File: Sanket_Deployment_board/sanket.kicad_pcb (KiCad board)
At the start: 2 copper layers, 95.9 x 92 mm, 42 parts, among them J2 Conn_02x03_Counter_Clockwise, J3 Conn_02x03_Counter_Clockwise, U1 SN74LVC1G17QDCKRQ1

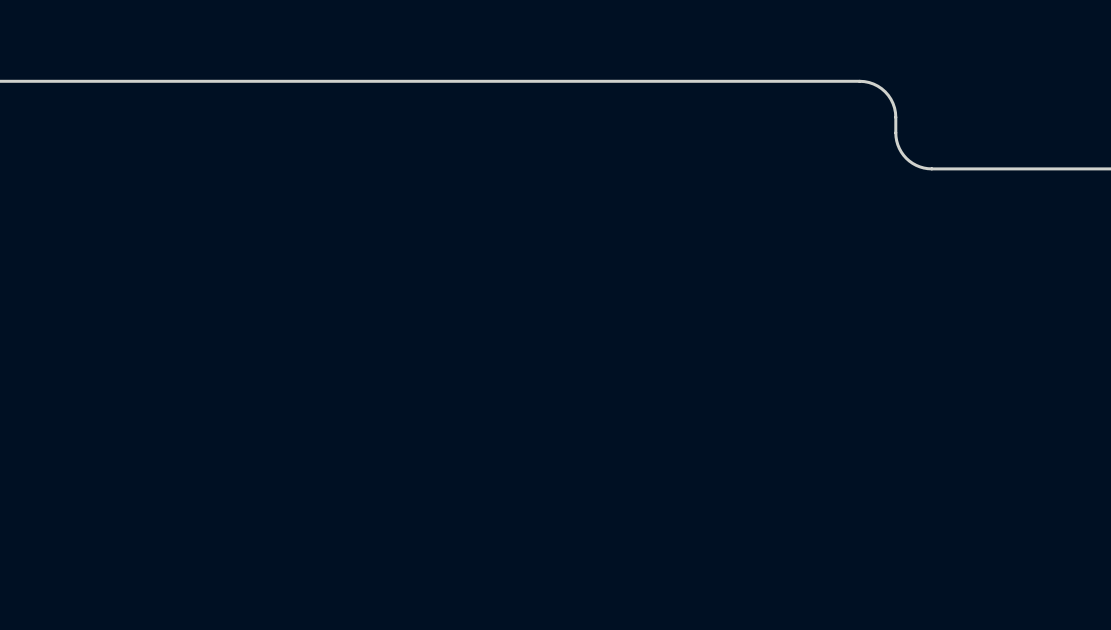
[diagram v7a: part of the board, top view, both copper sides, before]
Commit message: Added schematic pdf of Sanket
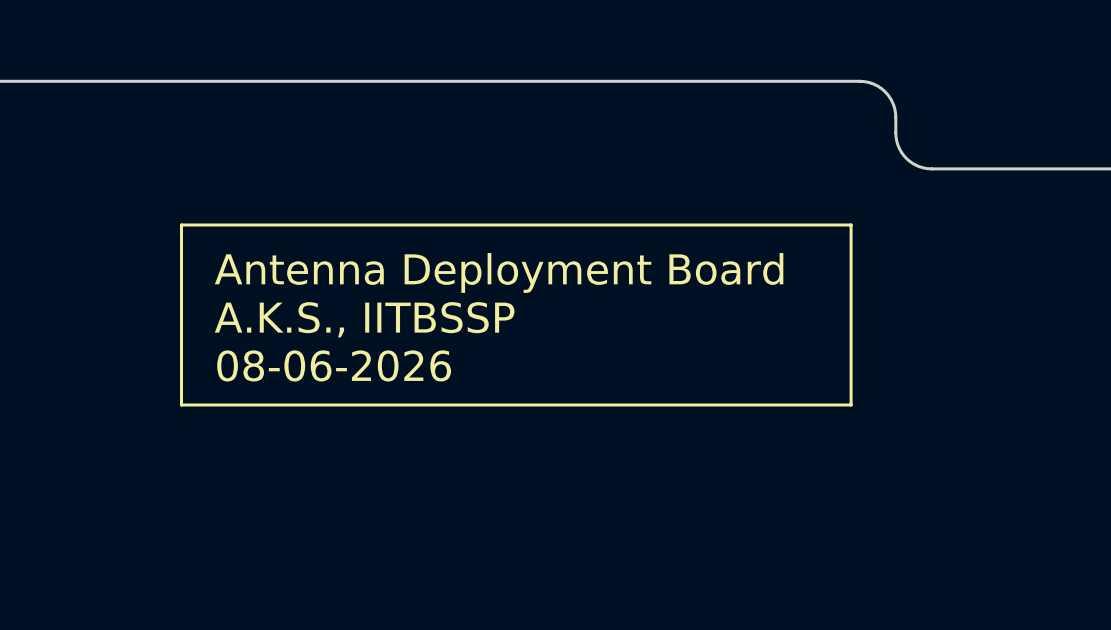
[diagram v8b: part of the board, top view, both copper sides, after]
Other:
- board text added: "Antenna Deployment Board A.K.S., IITBSSP 08-06-2026"
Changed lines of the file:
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@@
 	(paper "A4")
 	(title_block
-		(title "Antenna Deployment Board")
+		(title "ADS")
 		(date "2025-07-10")
 		(rev "6")
 		(company "IITBSSP")
+		(comment 1 "Author: A.K.S.")
 	)
 	(layers
@@
 		(embedded_fonts no)
 	)
+	(gr_rect
+		(start 114.4911 62.0886)
+		(end 136.8111 68.0886)
+		(stroke
+			(width 0.1)
+			(type default)
+		)
+		(fill no)
+		(layer "F.SilkS")
+	)
 	(gr_line
 		(start 100.4911 58.4986)
@@
 		(layer "Edge.Cuts")
 	)
+	(gr_text "Antenna Deployment Board\nA.K.S., IITBSSP\n08-06-2026"
+		(at 115.5911 67.4086 0)
+		(layer "F.SilkS")
+		(effects
+			(font
+				(size 1 1)
+				(thickness 0.1)
+			)
+			(justify left bottom)
+		)
+	)
 	(gr_text "12V"
 		(at 116.2411 131.0486 0)
@@
 	)
 	(zone
-		(net "/BurnWire1OUT")
+		(net "+3V3")
 		(layer "F.Cu")
 		(hatch none 0.1)
-		(priority 30001)
+		(priority 30004)
 		(attr
 			(teardrop
@@
 		(polygon
 			(pts
-				(xy 174.922166 106.9386) (xy 174.922166 105.9386) (xy 173.473001 105.625201) (xy 173.221166 106.4386)
-				(xy 173.473001 107.251999)
+				(xy 126.727839 128.802772) (xy 126.727839 129.202772) (xy 127.286114 129.300205) (xy 127.328839 129.002772)
+				(xy 127.286114 128.705339)
 			)
 		)
 	)
 	(zone
-		(net "/BurnWire1OUT")
+		(net "+12V")
 		(layer "F.Cu")
 		(hatch none 0.1)
-		(priority 30002)
+		(priority 30000)
 		(attr
 			(teardrop
@@
 		(polygon
 			(pts
-				(xy 174.070352 105.9386) (xy 174.070352 106.9386) (xy 175.519517 107.251999) (xy 175.771352 106.4386)
-				(xy 175.519517 105.625201)
+				(xy 107.105694 133.941113) (xy 106.398587 133.234006) (xy 104.949018 134.1886) (xy 105.300393 135.039307)
+				(xy 106.1511 135.390682)
 			)
 		)
 	)
 	(zone
-		(net "+12V")
+		(net "+3V3")
 		(layer "F.Cu")
 		(hatch none 0.1)
-		(priority 30000)
+		(priority 30007)
 		(attr
 			(teardrop
@@
 		(polygon
 			(pts
-				(xy 107.105694 133.941113) (xy 106.398587 133.234006) (xy 104.949018 134.1886) (xy 105.300393 135.039307)
-				(xy 106.1511 135.390682)
+				(xy 125.965041 135.650338) (xy 126.106462 135.791759) (xy 126.573005 135.575764) (xy 126.460722 135.296078)
+				(xy 126.181036 135.183795)
 			)
 		)
 	)
 	(zone
-		(net "+3V3")
+		(net "/BurnWire1OUT")
 		(layer "F.Cu")
 		(hatch none 0.1)
-		(priority 30006)
+		(priority 30001)
 		(attr
 			(teardrop
@@
 		(polygon
 			(pts
-				(xy 125.3711 138.401167) (xy 125.1711 138.401167) (xy 124.993936 138.883795) (xy 125.2711 139.002167)
-				(xy 125.548264 138.883795)
+				(xy 174.922166 106.9386) (xy 174.922166 105.9386) (xy 173.473001 105.625201) (xy 173.221166 106.4386)
+				(xy 173.473001 107.251999)
 			)
 		)
@@
 		(layer "F.Cu")
 		(hatch none 0.1)
-		(priority 30005)
+		(priority 30006)
 		(attr
 			(teardrop
@@
 		(polygon
 			(pts
-				(xy 123.192127 127.61247) (xy 123.47497 127.329627) (xy 123.149106 126.865972) (xy 122.908578 127.046078)
-				(xy 122.728472 127.286606)
+				(xy 125.3711 138.401167) (xy 125.1711 138.401167) (xy 124.993936 138.883795) (xy 125.2711 139.002167)
+				(xy 125.548264 138.883795)
 			)
 		)
 	)
 	(zone
-		(net "+3V3")
+		(net "Net-(J1-Pin_1)")
 		(layer "F.Cu")
 		(hatch none 0.1)
-		(priority 30004)
+		(priority 30003)
 		(attr
 			(teardrop
@@
 		(polygon
 			(pts
-				(xy 126.727839 128.802772) (xy 126.727839 129.202772) (xy 127.286114 129.300205) (xy 127.328839 129.002772)
-				(xy 127.286114 128.705339)
+				(xy 127.9611 129.9286) (xy 127.9611 130.9286) (xy 128.8111 131.2786) (xy 129.6621 130.4286) (xy 128.8111 129.6286)
 			)
 		)
 	)
 	(zone
-		(net "Net-(J1-Pin_1)")
+		(net "+3V3")
 		(layer "F.Cu")
 		(hatch none 0.1)
-		(priority 30003)
+		(priority 30005)
 		(attr
 			(teardrop
@@
 		(polygon
 			(pts
-				(xy 127.9611 129.9286) (xy 127.9611 130.9286) (xy 128.8111 131.2786) (xy 129.6621 130.4286) (xy 128.8111 129.6286)
+				(xy 123.192127 127.61247) (xy 123.47497 127.329627) (xy 123.149106 126.865972) (xy 122.908578 127.046078)
+				(xy 122.728472 127.286606)
 			)
 		)
 	)
 	(zone
-		(net "+3V3")
+		(net "/BurnWire1OUT")
 		(layer "F.Cu")
 		(hatch none 0.1)
-		(priority 30007)
+		(priority 30002)
 		(attr
 			(teardrop
@@
 		(polygon
 			(pts
-				(xy 125.965041 135.650338) (xy 126.106462 135.791759) (xy 126.573005 135.575764) (xy 126.460722 135.296078)
-				(xy 126.181036 135.183795)
+				(xy 174.070352 105.9386) (xy 174.070352 106.9386) (xy 175.519517 107.251999) (xy 175.771352 106.4386)
+				(xy 175.519517 105.625201)
 			)
 		)
@@
 		(layer "B.Cu")
 		(hatch none 0.1)
-		(priority 30009)
+		(priority 30008)
 		(attr
 			(teardrop
@@
 		(polygon
 			(pts
-				(xy 122.7111 126.6286) (xy 123.1111 126.6286) (xy 123.4111 126.123627) (xy 122.9111 125.6276) (xy 122.4111 126.123627)
+				(xy 124.1361 125.6386) (xy 124.1361 125.2386) (xy 123.3861 125.1286) (xy 122.9101 125.4386) (xy 123.624165 125.9386)
 			)
 		)
@@
 		(layer "B.Cu")
 		(hatch none 0.1)
-		(priority 30004)
+		(priority 30000)
 		(attr
 			(teardrop
@@
 		(polygon
 			(pts
-				(xy 128.877001 142.907395) (xy 128.169895 143.614501) (xy 128.010796 143.7736) (xy 129.761807 144.499307)
-				(xy 130.061404 143.7736)
+				(xy 133.2361 144.9986) (xy 133.2361 143.9986) (xy 132.5111 143.7736) (xy 129.7601 144.4986) (xy 132.5111 145.2236)
 			)
 		)
@@
 		(layer "B.Cu")
 		(hatch none 0.1)
-		(priority 30007)
+		(priority 30009)
 		(attr
 			(teardrop
@@
 		(polygon
 			(pts
-				(xy 124.4227 141.0416) (xy 124.2227 141.0416) (xy 123.84173 141.695929) (xy 124.3227 142.2676) (xy 124.80367 141.695929)
+				(xy 122.7111 126.6286) (xy 123.1111 126.6286) (xy 123.4111 126.123627) (xy 122.9111 125.6276) (xy 122.4111 126.123627)
 			)
 		)
@@
 		(layer "B.Cu")
 		(hatch none 0.1)
-		(priority 30005)
+		(priority 30011)
 		(attr
 			(teardrop
@@
 		(polygon
 			(pts
-				(xy 125.205854 139.205267) (xy 125.064433 139.063846) (xy 124.137316 139.4076) (xy 124.241693 140.028007)
-				(xy 124.8352 140.159285)
+				(xy 124.777941 139.350338) (xy 124.919362 139.491759) (xy 125.385905 139.275764) (xy 125.273622 138.996078)
+				(xy 124.993936 138.883795)
 			)
 		)
@@
 		(layer "B.Cu")
 		(hatch none 0.1)
-		(priority 30011)
+		(priority 30007)
 		(attr
 			(teardrop
@@
 		(polygon
 			(pts
-				(xy 124.777941 139.350338) (xy 124.919362 139.491759) (xy 125.385905 139.275764) (xy 125.273622 138.996078)
-				(xy 124.993936 138.883795)
+				(xy 124.4227 141.0416) (xy 124.2227 141.0416) (xy 123.84173 141.695929) (xy 124.3227 142.2676) (xy 124.80367 141.695929)
 			)
 		)
@@
 		(layer "B.Cu")
 		(hatch none 0.1)
-		(priority 30008)
+		(priority 30004)
 		(attr
 			(teardrop
@@
 		(polygon
 			(pts
-				(xy 124.1361 125.6386) (xy 124.1361 125.2386) (xy 123.3861 125.1286) (xy 122.9101 125.4386) (xy 123.624165 125.9386)
+				(xy 128.877001 142.907395) (xy 128.169895 143.614501) (xy 128.010796 143.7736) (xy 129.761807 144.499307)
+				(xy 130.061404 143.7736)
 			)
 		)
 	)
 	(zone
-		(net "+3V3")
+		(net "GND")
 		(layer "B.Cu")
 		(hatch none 0.1)
-		(priority 30000)
+		(priority 30001)
 		(attr
 			(teardrop
@@
 		(polygon
 			(pts
-				(xy 133.2361 144.9986) (xy 133.2361 143.9986) (xy 132.5111 143.7736) (xy 129.7601 144.4986) (xy 132.5111 145.2236)
+				(xy 106.853841 129.112966) (xy 106.146734 128.405859) (xy 104.900413 129.208967) (xy 105.297499 129.962201)
+				(xy 106.050733 130.359287)
 			)
 		)
 	)
 	(zone
-		(net "+12V")
+		(net "+3V3")
 		(layer "B.Cu")
 		(hatch none 0.1)
-		(priority 30003)
+		(priority 30005)
 		(attr
 			(teardrop
@@
 		(polygon
 			(pts
-				(xy 107.0011 135.5386) (xy 107.0011 134.5386) (xy 106.1511 134.1886) (xy 105.3001 135.0386) (xy 106.1511 135.8886)
+				(xy 125.205854 139.205267) (xy 125.064433 139.063846) (xy 124.137316 139.4076) (xy 124.241693 140.028007)
+				(xy 124.8352 140.159285)
 			)
 		)
@@
 	)
 	(zone
-		(net "GND")
-		(layer "B.Cu")
-		(hatch edge 0.5)
-		(connect_pads
-			(clearance 0.2)
-		)
-		(min_thickness 0.25)
-		(fill yes
-			(thermal_gap 0.5)
-			(thermal_bridge_width 0.5)
-			(island_removal_mode 0)
-		)
-		(polygon
-			(pts
-				(xy 126.7811 128.3086) (xy 103.635272 128.360661) (xy 102.4011 138.4086) (xy 101.4011 142.5386)
-				(xy 102.97468 148.034891) (xy 114.017939 145.624399) (xy 124.4111 145.6386) (xy 124.5211 145.6386)
-				(xy 127.2411 132.3986)
-			)
-		)
-	)
-	(zone
-		(net "GND")
+		(net "+3V3")
 		(layer "B.Cu")
 		(hatch none 0.1)
-		(priority 30001)
+		(priority 30006)
 		(attr
 			(teardrop
@@
 		(polygon
 			(pts
-				(xy 106.853841 129.112966) (xy 106.146734 128.405859) (xy 104.900413 129.208967) (xy 105.297499 129.962201)
-				(xy 106.050733 130.359287)
+				(xy 124.2227 141.3201) (xy 124.4227 141.3201) (xy 124.81617 140.653271) (xy 124.3227 140.1066) (xy 123.82923 140.653271)
 			)
 		)
@@
 		(layer "B.Cu")
 		(hatch none 0.1)
-		(priority 30006)
+		(priority 30002)
 		(attr
 			(teardrop
@@
 		(polygon
 			(pts
-				(xy 124.2227 141.3201) (xy 124.4227 141.3201) (xy 124.81617 140.653271) (xy 124.3227 140.1066) (xy 123.82923 140.653271)
+				(xy 169.133518 107.284234) (xy 169.840625 107.991341) (xy 171.086946 107.188233) (xy 170.68986 106.434999)
+				(xy 169.936626 106.037913)
 			)
 		)
 	)
 	(zone
-		(net "+3V3")
+		(net "+12V")
 		(layer "B.Cu")
 		(hatch none 0.1)
-		(priority 30002)
+		(priority 30003)
 		(attr
 			(teardrop
@@
 		(polygon
 			(pts
-				(xy 169.133518 107.284234) (xy 169.840625 107.991341) (xy 171.086946 107.188233) (xy 170.68986 106.434999)
-				(xy 169.936626 106.037913)
+				(xy 107.0011 135.5386) (xy 107.0011 134.5386) (xy 106.1511 134.1886) (xy 105.3001 135.0386) (xy 106.1511 135.8886)
+			)
+		)
+	)
+	(zone
+		(net "GND")
+		(layer "B.Cu")
+		(hatch edge 0.5)
+		(connect_pads
+			(clearance 0.2)
+		)
+		(min_thickness 0.25)
+		(fill yes
+			(thermal_gap 0.5)
+			(thermal_bridge_width 0.5)
+			(island_removal_mode 0)
+		)
+		(polygon
+			(pts
+				(xy 126.7811 128.3086) (xy 103.635272 128.360661) (xy 102.4011 138.4086) (xy 101.4011 142.5386)
+				(xy 102.97468 148.034891) (xy 114.017939 145.624399) (xy 124.4111 145.6386) (xy 124.5211 145.6386)
+				(xy 127.2411 132.3986)
 			)
 		)
